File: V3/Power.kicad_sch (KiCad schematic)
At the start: 19 parts

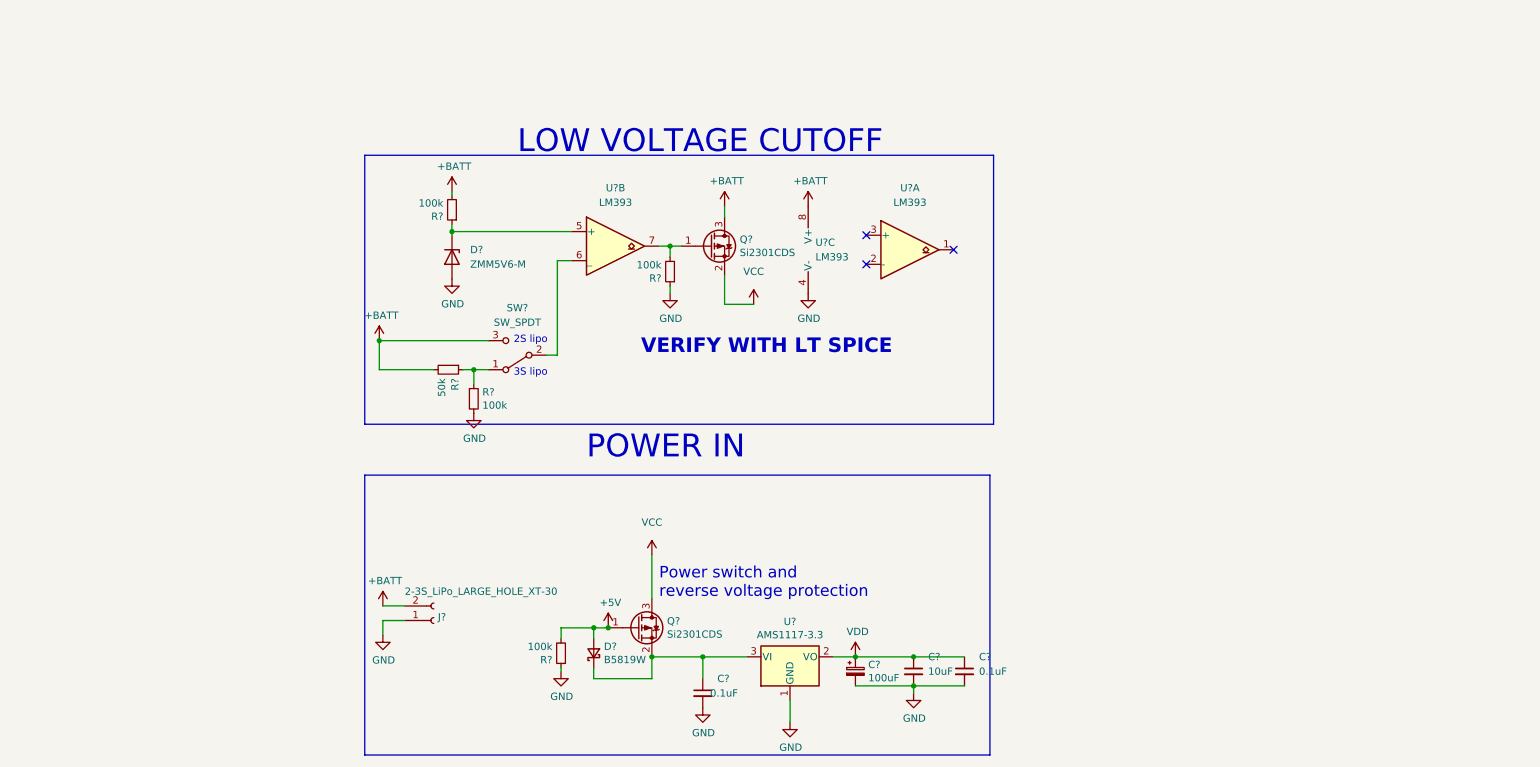
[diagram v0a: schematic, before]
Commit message: Added sims, updated V3 board
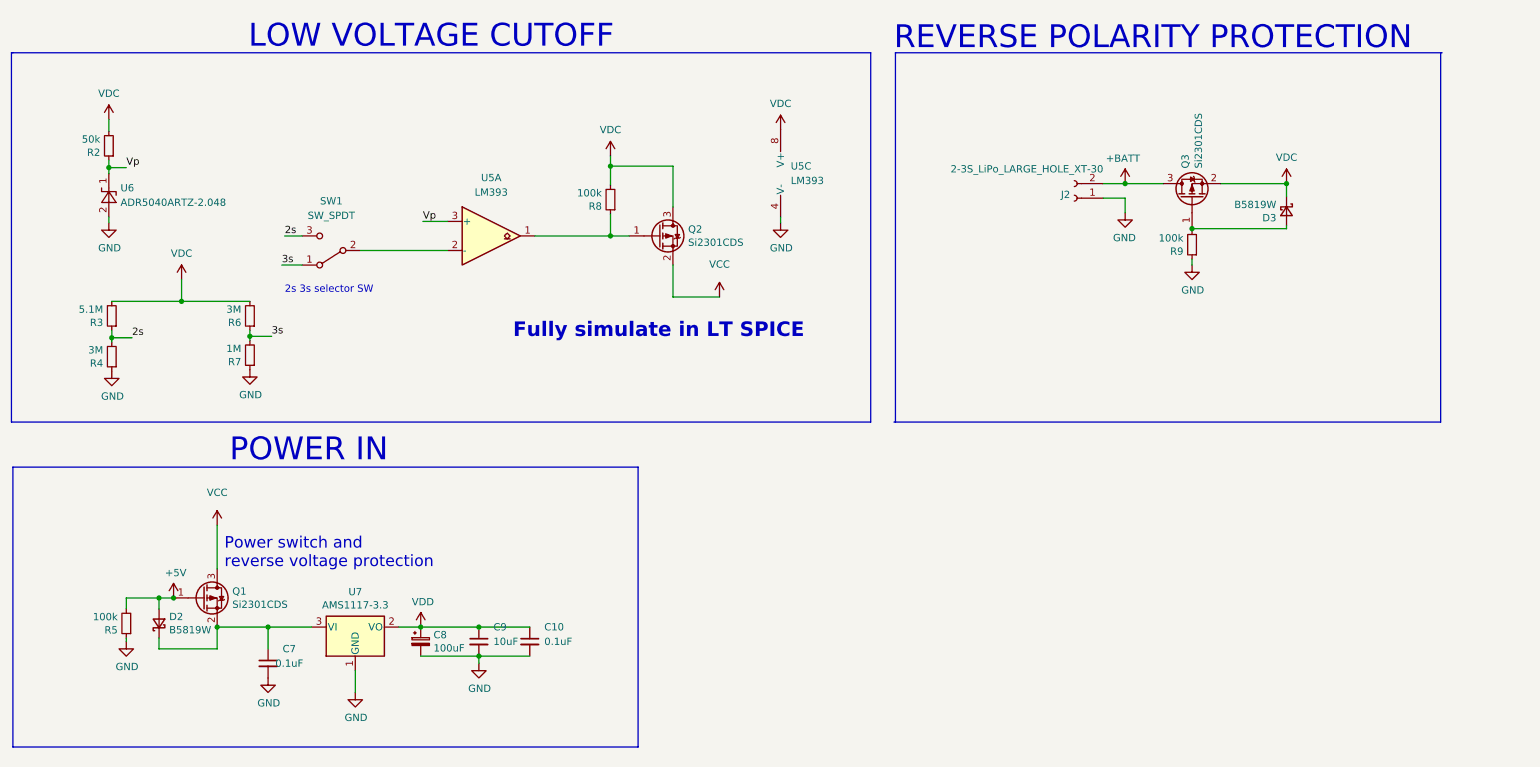
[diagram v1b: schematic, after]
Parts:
- removed D?: ZMM5V6-M, Diode_SMD:D_MiniMELF, symbol Diode:ZMMxx
- removed Q?: Si2301CDS, Package_TO_SOT_SMD:SOT-23, symbol Transistor_FET:Si2319CDS
- removed R?: 50k, Resistor_SMD:R_0603_1608Metric, symbol Device:R_Small
- removed R? (x3): 100k, Resistor_SMD:R_0603_1608Metric, symbol Device:R_Small
- removed SW?: SW_SPDT, Local_footprints:SSSS811101, symbol Switch:SW_SPDT
- removed U?: LM393, Local_footprints:LM393DR2G, symbol Comparator:LM393
- removed U? (x2): LM393, symbol Comparator:LM393
- added D3: B5819W, Diode_SMD:D_SOD-123, symbol Device:D_Schottky_Small
- added Q2, Q3: Si2301CDS, Package_TO_SOT_SMD:SOT-23, symbol Transistor_FET:Si2319CDS
- added R2: 50k, Resistor_SMD:R_0603_1608Metric, symbol Device:R_Small
- added R3: 5.1M, Resistor_SMD:R_0603_1608Metric, symbol Device:R_Small
- added R4, R6: 3M, Resistor_SMD:R_0603_1608Metric, symbol Device:R_Small
- added R7: 1M, Resistor_SMD:R_0603_1608Metric, symbol Device:R_Small
- added R8, R9: 100k, Resistor_SMD:R_0603_1608Metric, symbol Device:R_Small
- added SW1: SW_SPDT, Local_footprints:SSSS811101, symbol Switch:SW_SPDT
- added U5: LM393, Local_footprints:LM393DR2G, symbol Comparator:LM393
- added U6: ADR5040ARTZ-2.048, Local_footprints:Analog_Devices-ADR5040ARTZ-REEL7-Level_C, symbol Reference_Voltage:LM4040DBZ-2.0
- gave numbers to parts that had none: 9
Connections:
- net +BATT: now also Q3.3 (D)
- net GND: now also R4.1, R7.1, R9.1, U5.4 (V-), U6.2 (A)
- net VCC: now also Q2.2 (S)
- new net: D3.2 (A), Q3.1 (G), R9.2
- new net: Q2.1 (G), R8.1, U5.1
- new net: SW1.2 (B), U5.2 (-)
- new net 2s: R3.1, R4.2, SW1.3 (C)
- new net 3s: R6.1, R7.2, SW1.1 (A)
- new net VDC: D3.1 (K), Q2.3 (D), Q3.2 (S), R2.2, R3.2, R6.2, R8.2, U5.8 (V+)
- new net Vp: R2.1, U5.3 (+), U6.1 (K)
- no-connect marks 3 -> 0
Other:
- note added: "2s 3s selector SW"
- note added: "Fully simulate in LT SPICE"
- note added: "REVERSE POLARITY PROTECTION"
- note removed: "2S lipo"
- note removed: "3S lipo"
- note removed: "VERIFY WITH LT SPICE"
- moved on the sheet: C10, C7, C8, C9, D2, J2, Q1, R5, U7

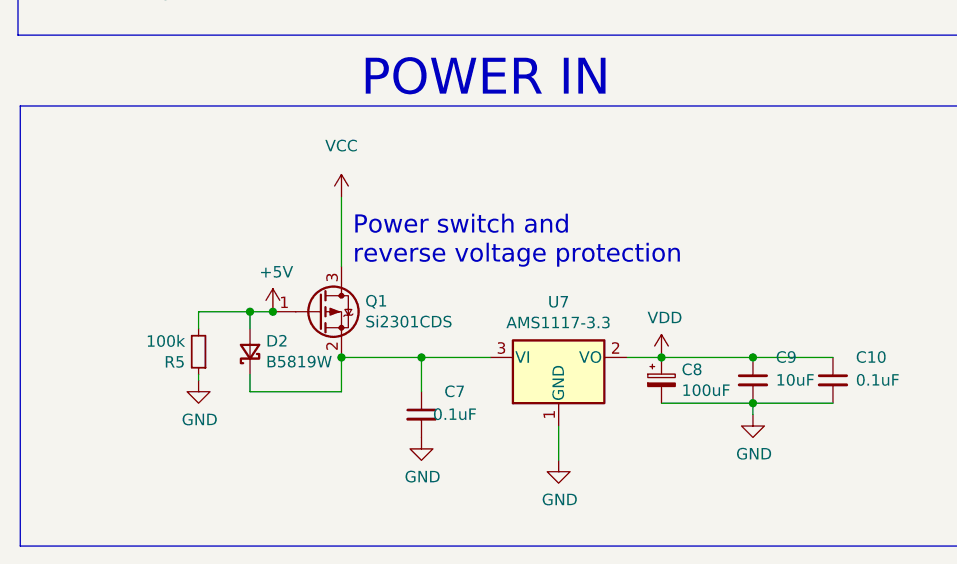
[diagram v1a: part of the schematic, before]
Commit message: Added mpu6050 back
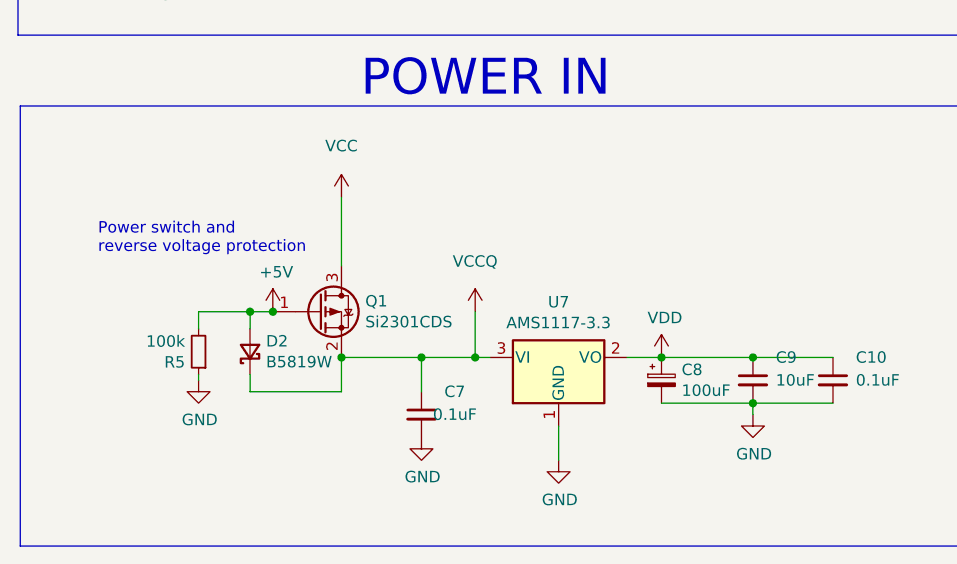
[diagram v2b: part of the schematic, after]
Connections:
- net VCCQ: now reaches C7.1, D2.1 (K), Q1.2 (S), U7.3 (VI)
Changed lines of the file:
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@@
   (junction (at 105.029 119.888) (diameter 0) (color 0 0 0 0)
   )
+  (junction (at 84.328 119.888) (diameter 0) (color 0 0 0 0)
+  )
   (junction (at 78.359 119.888) (diameter 0) (color 0 0 0 0)
   )
@@
     (stroke (width 0) (type default) (color 0 0 0 0))
   )
+  (wire (pts (xy 84.328 114.808) (xy 84.328 119.888))
+    (stroke (width 0) (type default) (color 0 0 0 0))
+  )
   (wire (pts (xy 101.219 119.888) (xy 105.029 119.888))
     (stroke (width 0) (type default) (color 0 0 0 0))
@@
     (stroke (width 0) (type default) (color 0 0 0 0))
   )
+  (wire (pts (xy 84.328 119.888) (xy 85.979 119.888))
+    (stroke (width 0) (type default) (color 0 0 0 0))
+  )
   (polyline (pts (xy 283.21 84.074) (xy 187.706 84.074))
     (stroke (width 0) (type default) (color 0 0 0 0))
@@
     (stroke (width 0) (type default) (color 0 0 0 0))
   )
-  (wire (pts (xy 78.359 119.888) (xy 85.979 119.888))
+  (wire (pts (xy 78.359 119.888) (xy 84.328 119.888))
     (stroke (width 0) (type default) (color 0 0 0 0))
   )
@@
     (stroke (width 0) (type default) (color 0 0 0 0))
   )
-  (text "Power switch and \nreverse voltage protection" (at 70.739 109.728 0)
-    (effects (font (size 2.0066 2.0066)) (justify left bottom))
+  (text "Power switch and \nreverse voltage protection" (at 42.418 108.458 0)
+    (effects (font (size 1.27 1.27)) (justify left bottom))
   )
   (text "LOW VOLTAGE CUTOFF" (at 74.93 19.05 0)
@@
     (pin "2")
   )
+  (symbol (lib_id "power:VCCQ") (at 84.328 114.808 0) (unit 1)
+    (in_bom yes) (on_board yes) (fields_autoplaced)
+    (property "Reference" "#PWR?" (id 0) (at 84.328 118.618 0)
+      (effects (font (size 1.27 1.27)) hide)
+    )
+    (property "Value" "VCCQ" (id 1) (at 84.328 109.22 0))
+    (property "Footprint" "" (id 2) (at 84.328 114.808 0)
+      (effects (font (size 1.27 1.27)) hide)
+    )
+    (property "Datasheet" "" (id 3) (at 84.328 114.808 0)
+      (effects (font (size 1.27 1.27)) hide)
+    )
+    (pin "1")
+  )
   (symbol (lib_id "power:GND") (at 115.189 126.238 0) (unit 1)

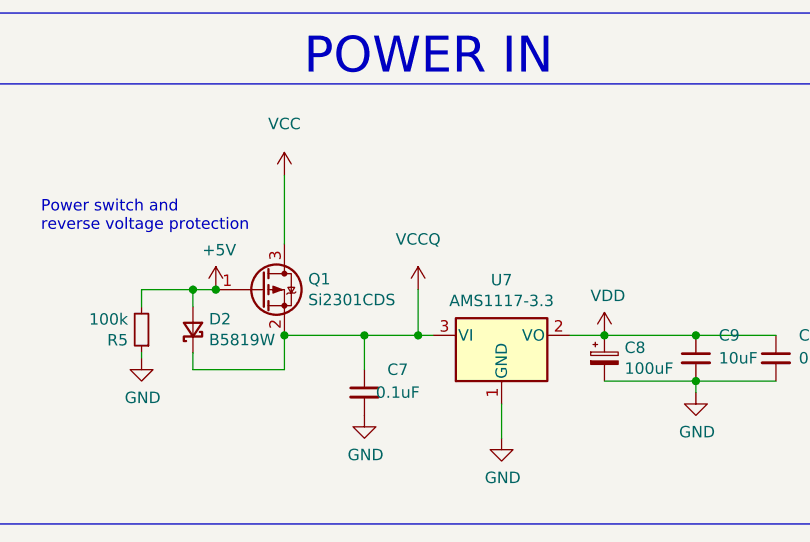
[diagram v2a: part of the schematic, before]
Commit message: buzzer added
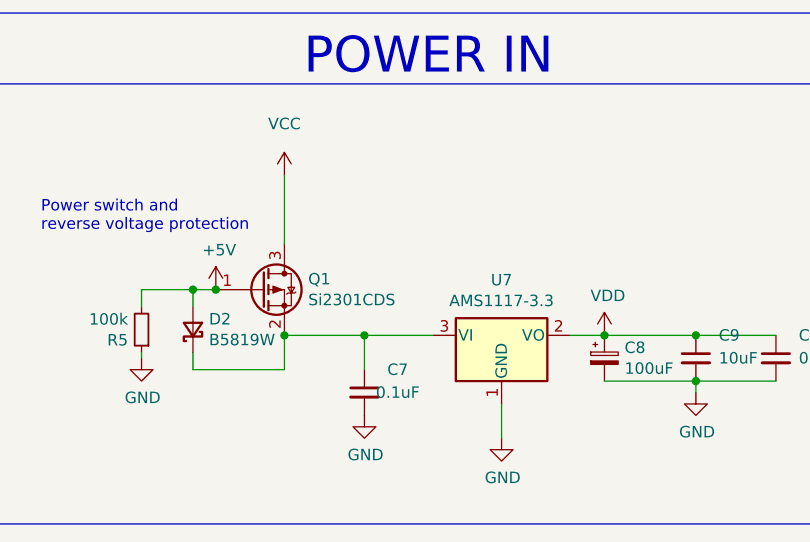
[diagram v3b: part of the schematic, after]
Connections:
- net VCCQ: no longer names the net of C7.1, D2.1 (K), Q1.2 (S), U7.3 (VI)
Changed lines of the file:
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@@
   (junction (at 105.029 119.888) (diameter 0) (color 0 0 0 0)
   )
-  (junction (at 84.328 119.888) (diameter 0) (color 0 0 0 0)
-  )
   (junction (at 78.359 119.888) (diameter 0) (color 0 0 0 0)
   )
@@
     (stroke (width 0) (type default) (color 0 0 0 0))
   )
-  (wire (pts (xy 84.328 114.808) (xy 84.328 119.888))
-    (stroke (width 0) (type default) (color 0 0 0 0))
-  )
   (wire (pts (xy 101.219 119.888) (xy 105.029 119.888))
     (stroke (width 0) (type default) (color 0 0 0 0))
@@
     (stroke (width 0) (type default) (color 0 0 0 0))
   )
-  (wire (pts (xy 84.328 119.888) (xy 85.979 119.888))
+  (wire (pts (xy 78.359 119.888) (xy 85.979 119.888))
     (stroke (width 0) (type default) (color 0 0 0 0))
   )
@@
   )
   (wire (pts (xy 115.189 119.888) (xy 124.079 119.888))
-    (stroke (width 0) (type default) (color 0 0 0 0))
-  )
-  (wire (pts (xy 78.359 119.888) (xy 84.328 119.888))
     (stroke (width 0) (type default) (color 0 0 0 0))
   )
@@
     (pin "2")
   )
-  (symbol (lib_id "power:VCCQ") (at 84.328 114.808 0) (unit 1)
-    (in_bom yes) (on_board yes) (fields_autoplaced)
-    (property "Reference" "#PWR?" (id 0) (at 84.328 118.618 0)
-      (effects (font (size 1.27 1.27)) hide)
-    )
-    (property "Value" "VCCQ" (id 1) (at 84.328 109.22 0))
-    (property "Footprint" "" (id 2) (at 84.328 114.808 0)
-      (effects (font (size 1.27 1.27)) hide)
-    )
-    (property "Datasheet" "" (id 3) (at 84.328 114.808 0)
-      (effects (font (size 1.27 1.27)) hide)
-    )
-    (pin "1")
-  )
   (symbol (lib_id "power:GND") (at 115.189 126.238 0) (unit 1)

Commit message: Updated costing sheet:
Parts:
- R2: value 50k -> 56k
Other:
- note removed: "Fully simulate in LT SPICE"
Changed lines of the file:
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@@
     (effects (font (size 3.9878 3.9878)) (justify left bottom))
-  )
-  (text "Fully simulate in LT SPICE" (at 121.158 69.596 0)
-    (effects (font (size 2.54 2.54) (thickness 0.508) bold) (justify left bottom))
   )
   (text "REVERSE POLARITY PROTECTION" (at 187.706 19.304 0)
@@
       (effects (font (size 1.27 1.27)) (justify left))
     )
-    (property "Value" "50k" (id 1) (at 49.0474 34.671 0)
+    (property "Value" "56k" (id 1) (at 49.0474 34.671 0)
       (effects (font (size 1.27 1.27)) (justify left))
     )

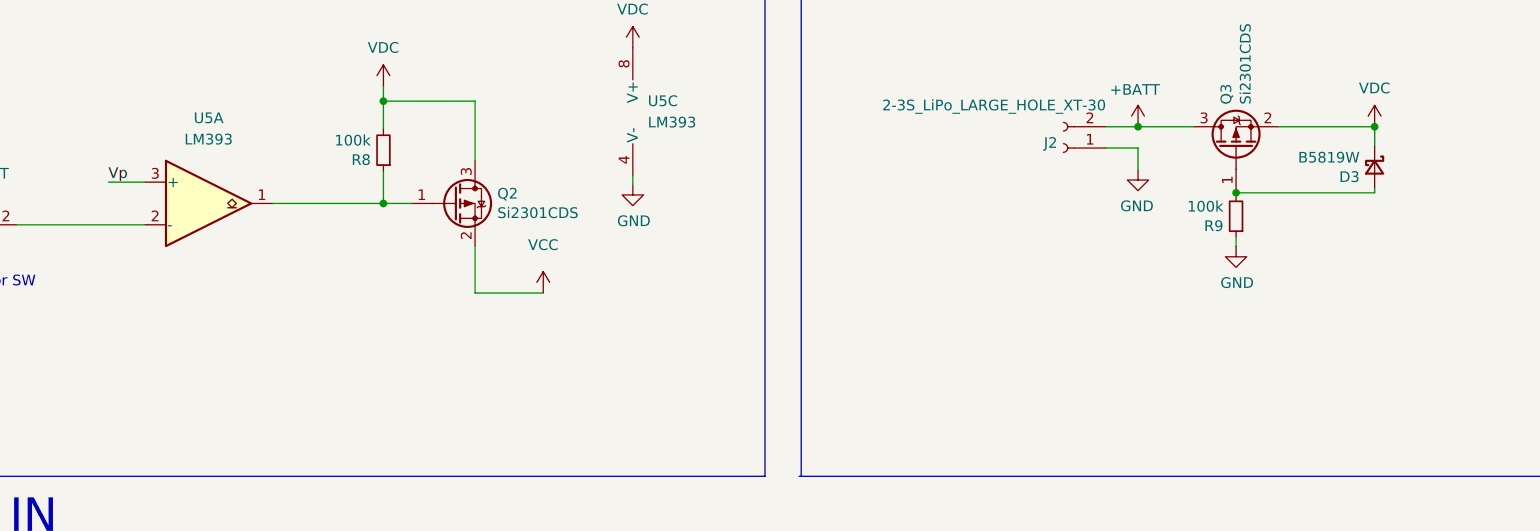
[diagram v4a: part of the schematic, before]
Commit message: Switched orentation of LVCO P-ch mosfet
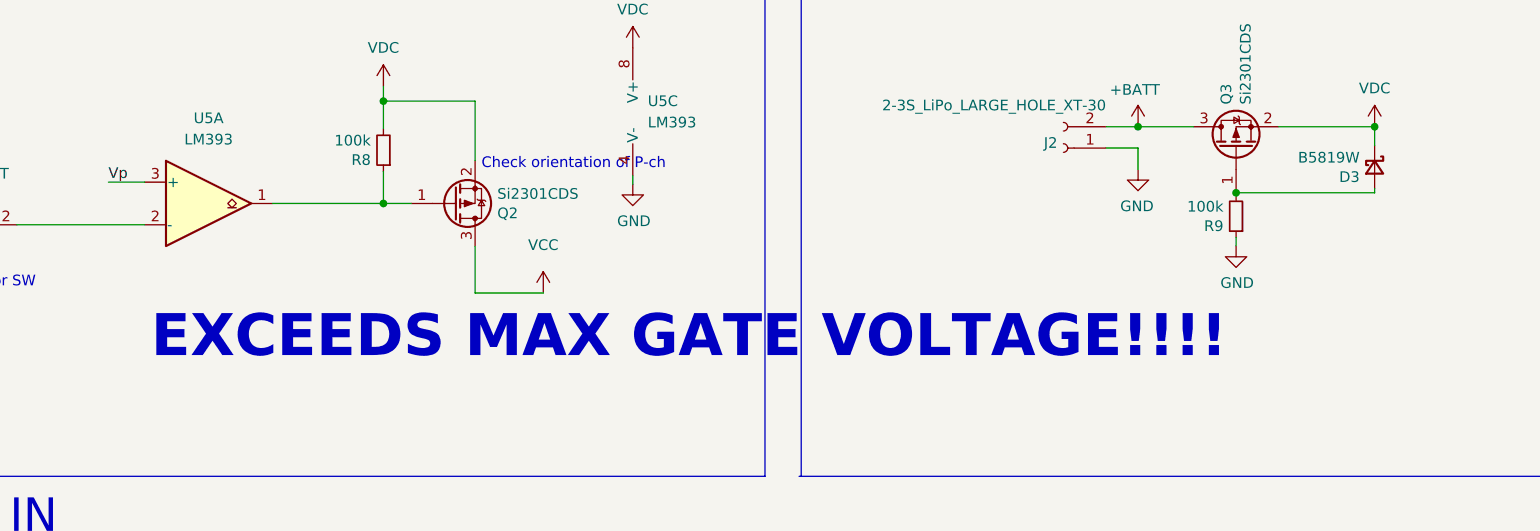
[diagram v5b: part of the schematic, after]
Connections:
- net VCC: now also Q2.3 (D); no longer Q2.2 (S)
- net VDC: now also Q2.2 (S); no longer Q2.3 (D)
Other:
- note added: "Check orientation of P-ch"
- note added: "EXCEEDS MAX GATE VOLTAGE!!!!"
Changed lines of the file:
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@@
     (stroke (width 0) (type default) (color 0 0 0 0))
+  )
+  (text "EXCEEDS MAX GATE VOLTAGE!!!!" (at 110.49 70.485 0)
+    (effects (font (size 5 5) (thickness 1) bold) (justify left bottom))
   )
   (text "Power switch and \nreverse voltage protection" (at 42.418 108.458 0)
@@
   (text "LOW VOLTAGE CUTOFF" (at 74.93 19.05 0)
     (effects (font (size 3.9878 3.9878)) (justify left bottom))
+  )
+  (text "Check orientation of P-ch" (at 149.86 47.625 0)
+    (effects (font (size 1.27 1.27)) (justify left bottom))
   )
   (text "REVERSE POLARITY PROTECTION" (at 187.706 19.304 0)
@@
     (pin "3")
   )
-  (symbol (lib_id "Transistor_FET:Si2319CDS") (at 146.558 51.562 0) (unit 1)
-    (in_bom yes) (on_board yes)
-    (property "Reference" "Q2" (id 0) (at 151.7396 50.3936 0)
-      (effects (font (size 1.27 1.27)) (justify left))
-    )
-    (property "Value" "Si2301CDS" (id 1) (at 151.7396 52.705 0)
-      (effects (font (size 1.27 1.27)) (justify left))
-    )
-    (property "Footprint" "Package_TO_SOT_SMD:SOT-23" (id 2) (at 151.638 53.467 0)
+  (symbol (lib_id "Transistor_FET:Si2319CDS") (at 146.558 51.562 0) (mirror x) (unit 1)
+    (in_bom yes) (on_board yes)
+    (property "Reference" "Q2" (id 0) (at 151.7396 52.7304 0)
+      (effects (font (size 1.27 1.27)) (justify left))
+    )
+    (property "Value" "Si2301CDS" (id 1) (at 151.7396 50.419 0)
+      (effects (font (size 1.27 1.27)) (justify left))
+    )
+    (property "Footprint" "Package_TO_SOT_SMD:SOT-23" (id 2) (at 151.638 49.657 0)
       (effects (font (size 1.27 1.27) italic) (justify left) hide)
     )
